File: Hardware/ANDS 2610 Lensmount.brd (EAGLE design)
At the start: 30.5 x 33 mm, 9 parts, among them Q1 24mhz, Q2 MMBT4403

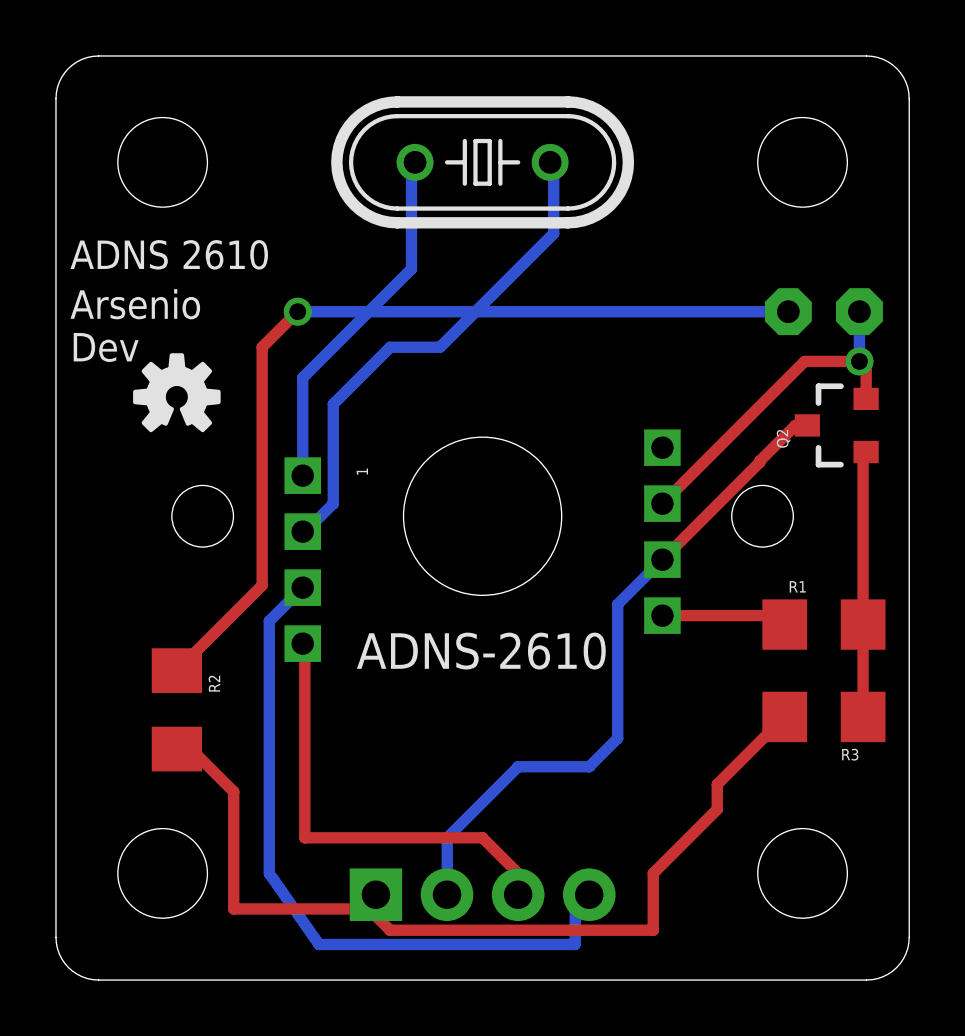
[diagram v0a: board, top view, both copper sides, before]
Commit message: Fixed trace
Had a trace crossing the Crystal leads
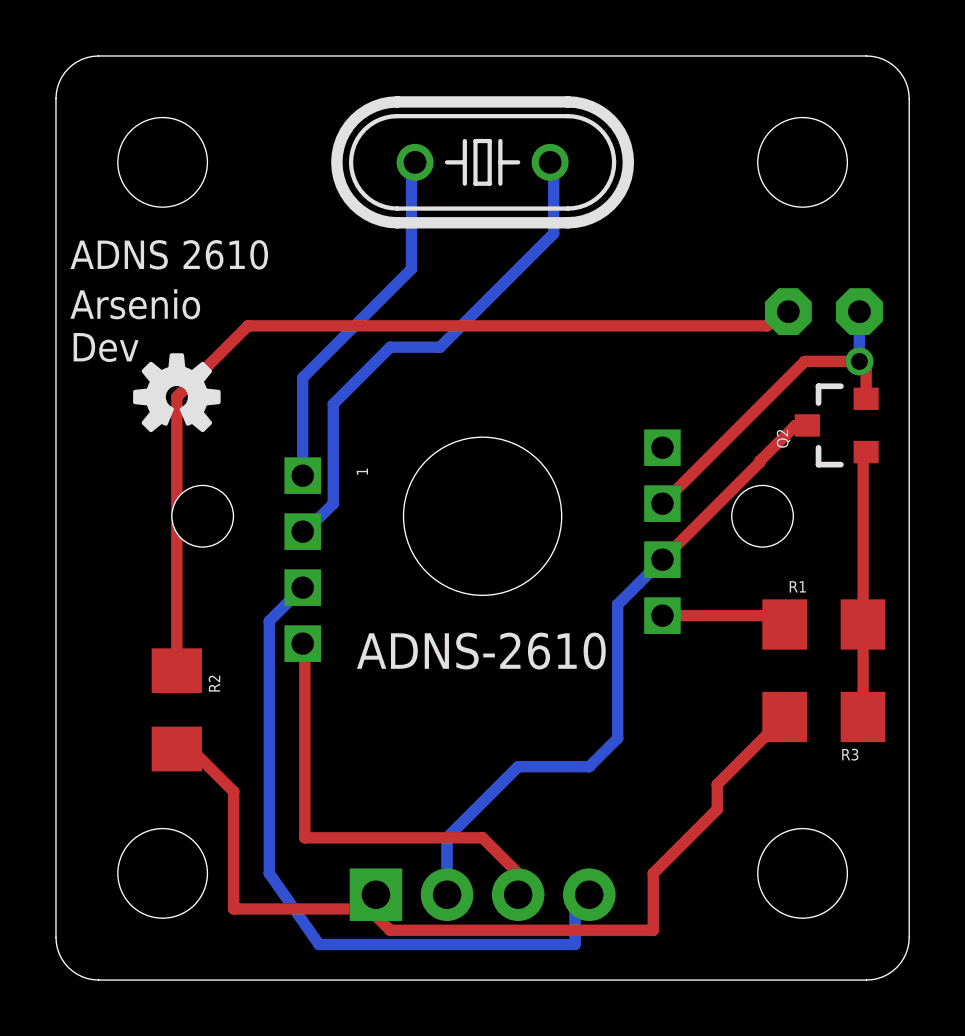
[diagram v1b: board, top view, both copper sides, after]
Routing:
- net N$6: track 32.1 -> 32.8 mm, vias 1 -> 0
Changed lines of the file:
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@@
 <contactref element="LED1" pad="A"/>
 <contactref element="R2" pad="1"/>
-<wire x1="17.018" y1="22.482" x2="20.066" y2="25.53" width="0.4064" layer="1"/>
-<wire x1="20.066" y1="25.53" x2="20.066" y2="34.036" width="0.4064" layer="1"/>
-<wire x1="20.066" y1="34.036" x2="21.336" y2="35.306" width="0.4064" layer="1"/>
-<wire x1="21.336" y1="35.306" x2="38.862" y2="35.306" width="0.4064" layer="16"/>
-<via x="21.336" y="35.306" extent="1-16" drill="0.6" shape="square"/>
+<wire x1="17.018" y1="22.482" x2="17.018" y2="32.258" width="0.4064" layer="1"/>
+<wire x1="17.018" y1="32.258" x2="19.558" y2="34.798" width="0.4064" layer="1"/>
+<wire x1="19.558" y1="34.798" x2="38.1" y2="34.798" width="0.4064" layer="1"/>
+<wire x1="38.1" y1="34.798" x2="38.862" y2="35.306" width="0.4064" layer="1"/>
 </signal>
 <signal name="N$7">
